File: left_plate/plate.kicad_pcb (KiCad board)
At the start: 2 copper layers, 146 x 96 mm, 23 parts

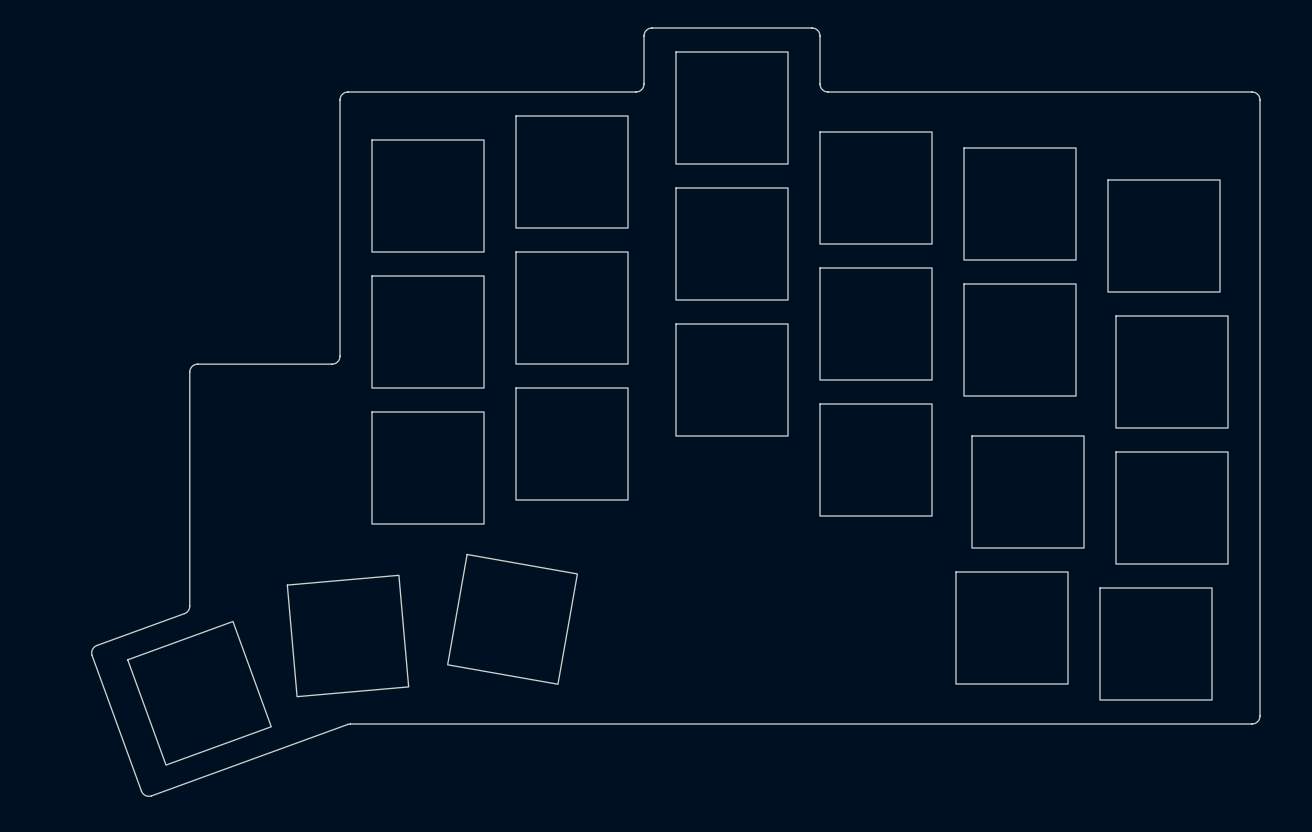
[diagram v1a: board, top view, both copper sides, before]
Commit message: adjust LED footprint to T1 standard
update plates and traces
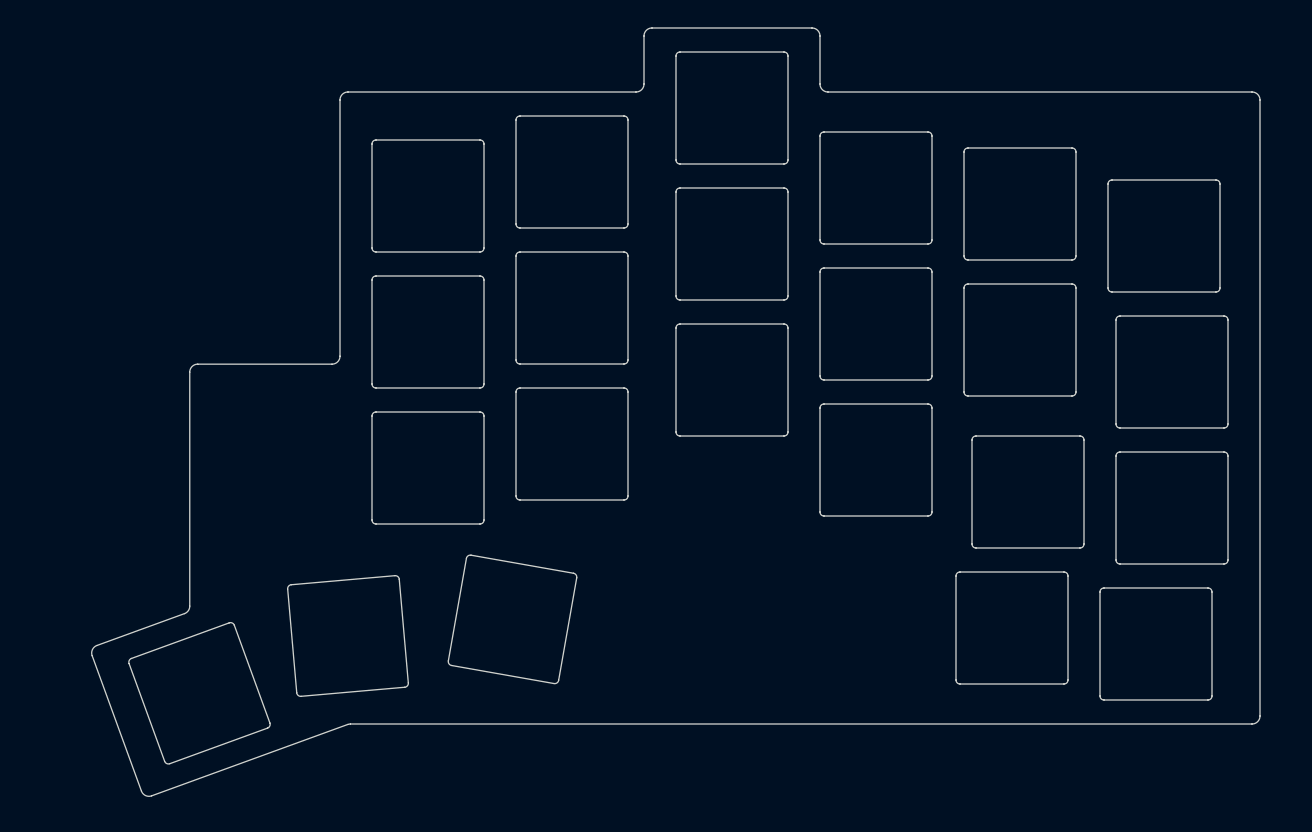
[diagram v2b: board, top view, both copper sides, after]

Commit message: add copper fill to plates and correct plate silkscreen
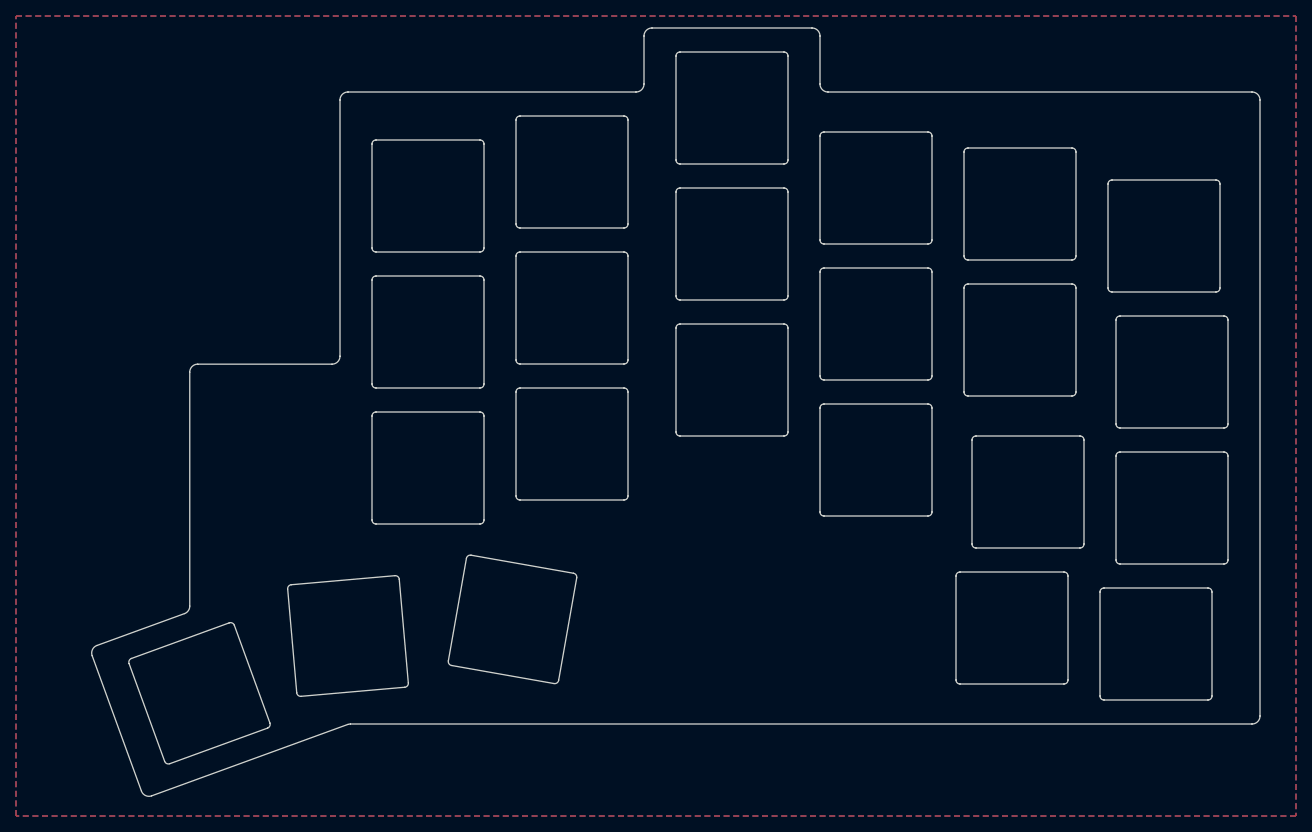
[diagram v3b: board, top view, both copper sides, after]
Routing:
- added copper zone on B.Cu, net (none)
- added copper zone on F.Cu, net (none)
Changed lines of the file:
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@@
   (gr_line (start 69.5 83.52) (end 52.72 83.52)
     (stroke (width 0.1) (type solid)) (layer "Edge.Cuts"))
+  (zone (net 0) (net_name "") (layers "F&B.Cu") (hatch edge 0.5)
+    (connect_pads (clearance 0.5))
+    (min_thickness 0.25) (filled_areas_thickness no)
+    (fill yes (thermal_gap 0.5) (thermal_bridge_width 0.5) (island_removal_mode 1) (island_area_min 10))
+    (polygon
+      (pts
+        (xy 190 40)
+        (xy 190 140)
+        (xy 30 140)
+        (xy 30 40)
+      )
+    )
+  )
 )

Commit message: update plates with asymmetrical pinky stagger
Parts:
- SW16, SW26, SW35, SW36, SW45, SW46: footprint Plate:Switch -> Plate:SwitchUp
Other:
- outline, holes or cut-outs redrawn
